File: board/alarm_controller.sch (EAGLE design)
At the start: 144 parts, among them IC3 AT24C, X1 RJ45-8L21-S, X2 RJ45-8L21-S

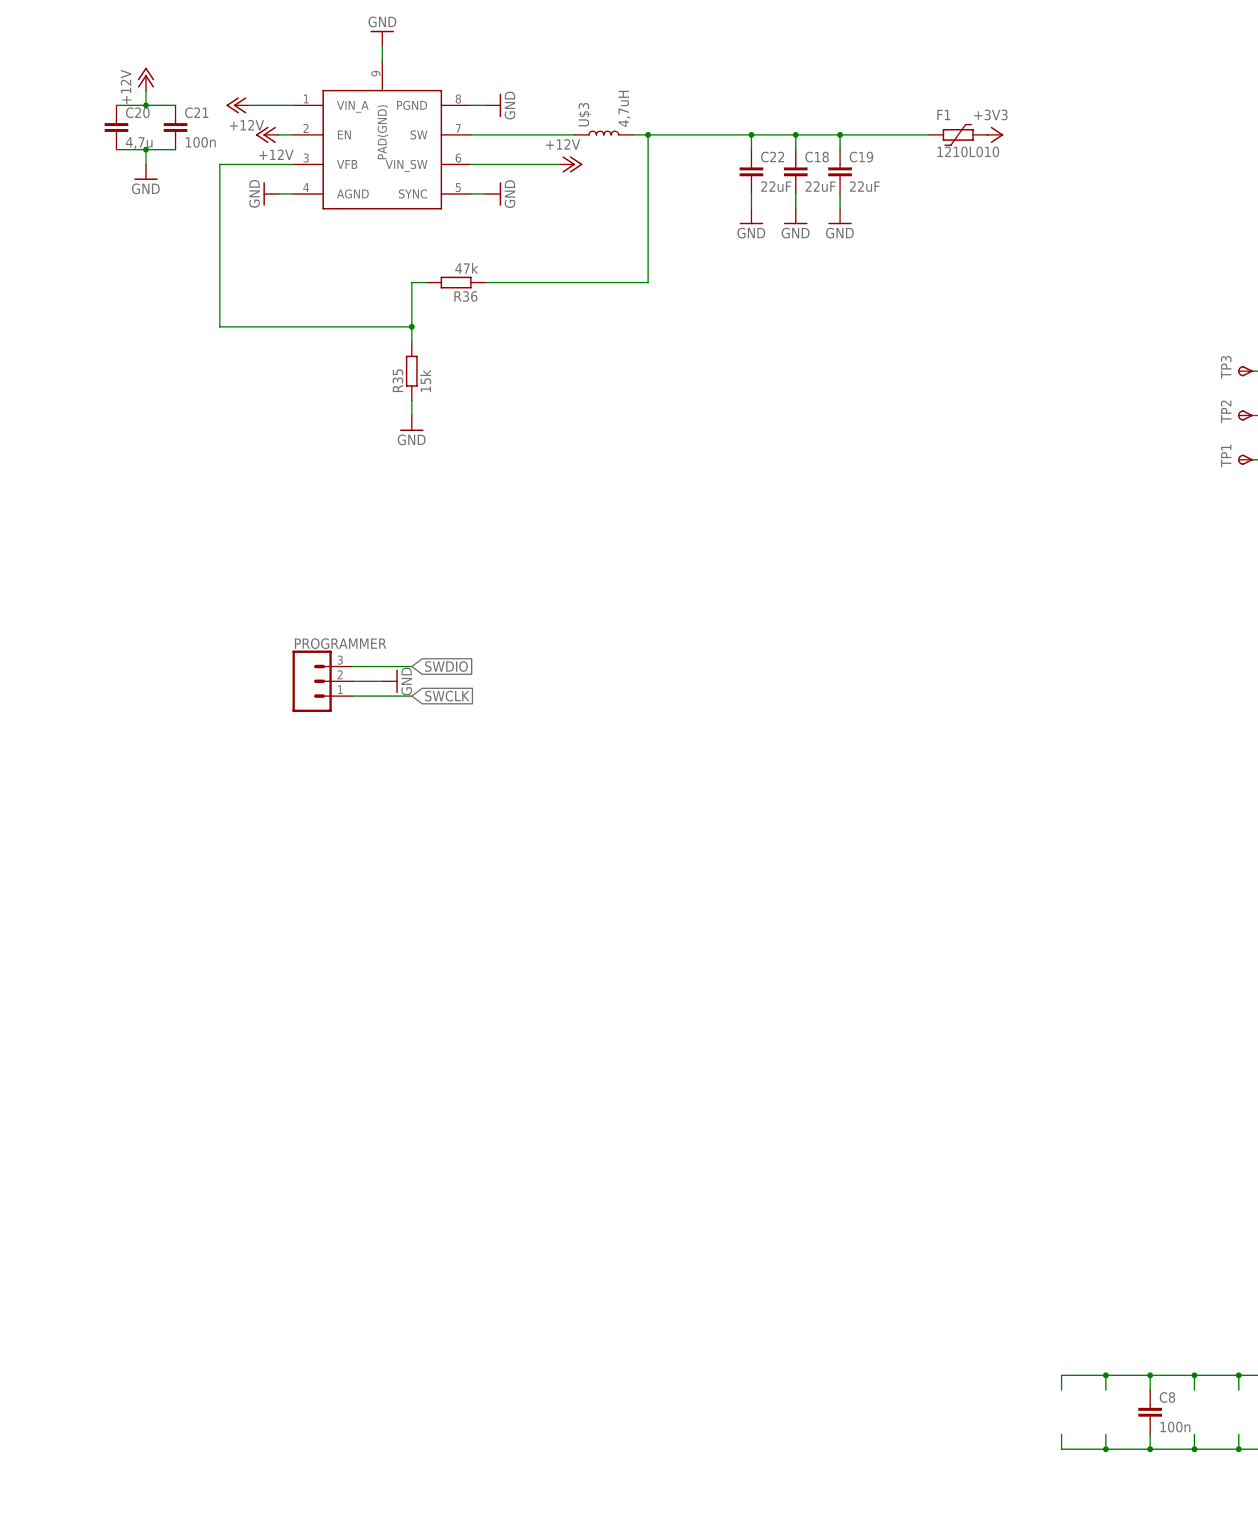
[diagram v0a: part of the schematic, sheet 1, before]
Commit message: change to premade power supply
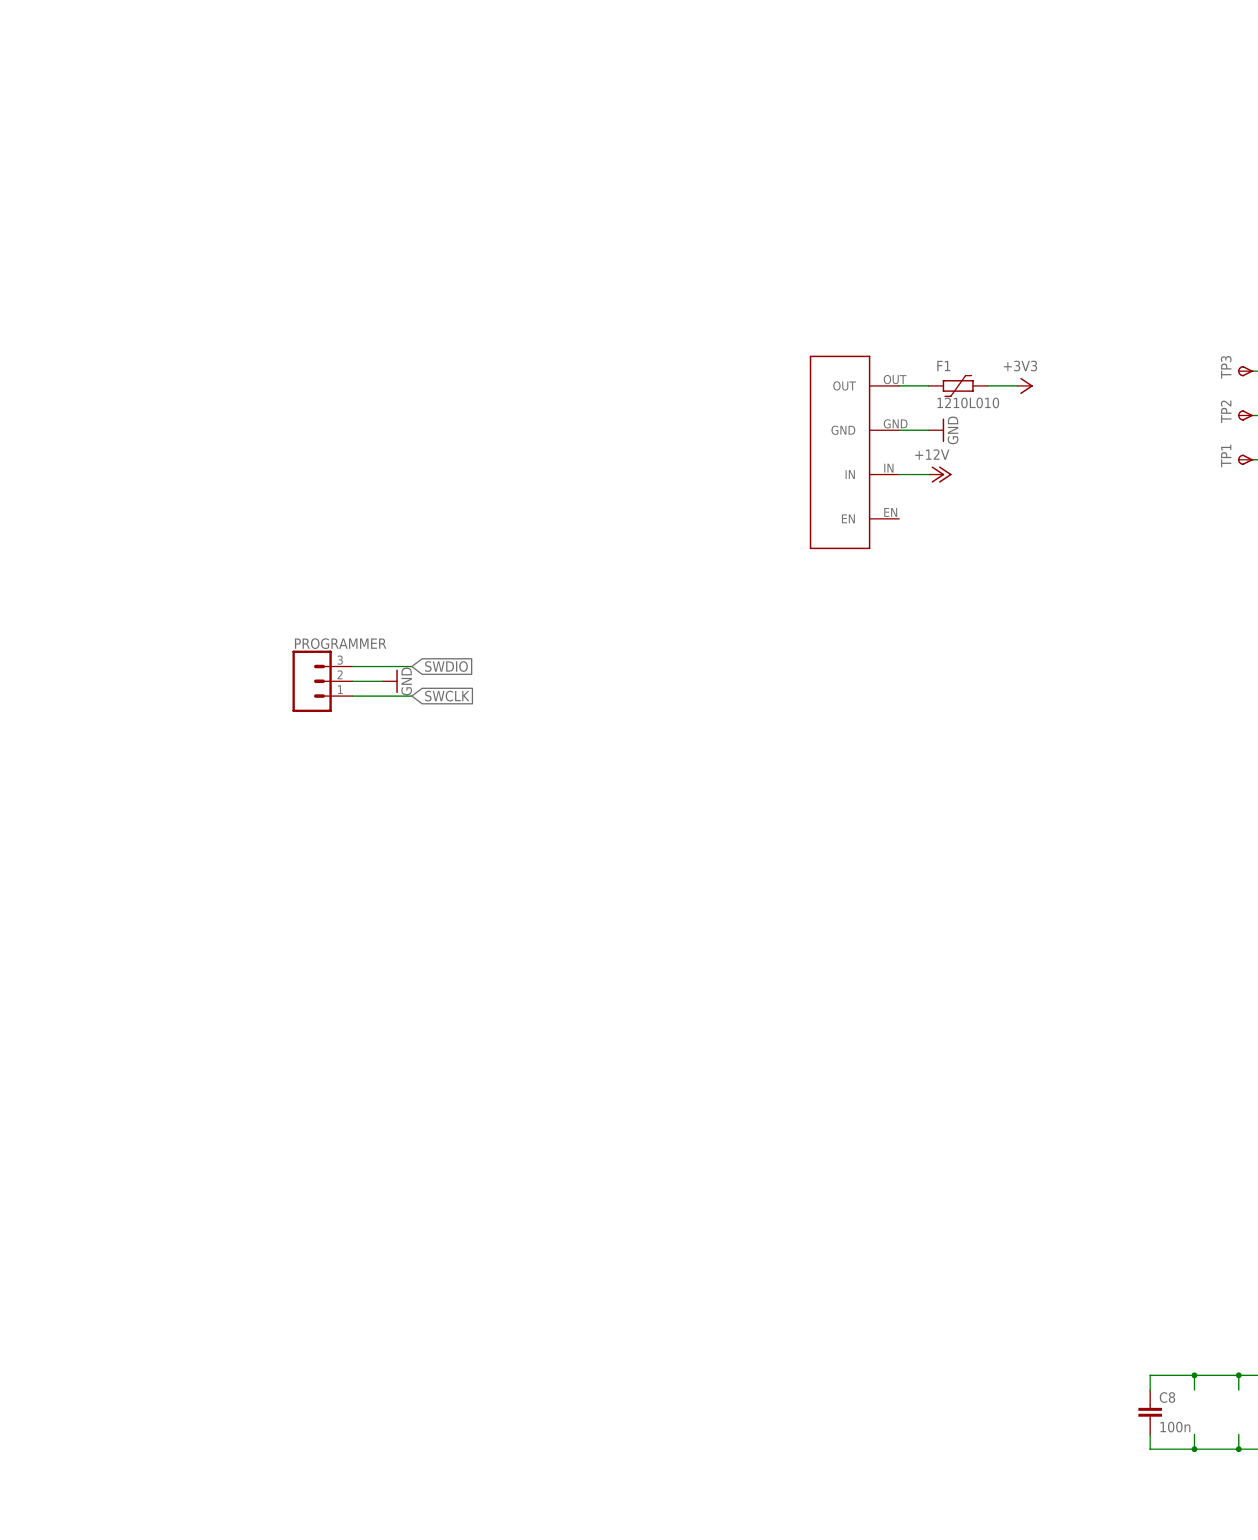
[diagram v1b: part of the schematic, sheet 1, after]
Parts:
- removed C18, C19, C22: 22uF, rcl:C-EUC0805
- removed C20: 4,7u, rcl:C-EUC1206
- removed C21: 100n, rcl:C-EUC0603
- removed R35: 15k, rcl:R-EU_R0603
- removed R36: 47k, rcl:R-EU_R0603
- removed U$2: ST1S10, lcd:ST1S10
- removed U$3: 4,7uH, lcd:PCD0504MT4R7
- added U$4: HW-613, components:HW-613
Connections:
- removed net N$13: C18.1, C19.1, C22.1, F1.2, R36.1, U$3.2
- removed net N$7: U$2.SW, U$3.1
- net +12V: now also U$4.IN; no longer C20.1, C21.1, U$2.EN, U$2.VIN_A, U$2.VIN_SW
- net GND: now also U$4.GND; no longer C18.2, C19.2, C20.2, C21.2, C22.2, R35.1, U$2.AGND, U$2.PAD(GND), U$2.PGND, U$2.SYNC
- net N$3: now also F1.2, U$4.OUT; no longer R35.2, R36.2, U$2.VFB
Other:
- moved on the sheet: F1

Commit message: add reset button
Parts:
- added S1: (no value), SparkFun-Switches:MOMENTARY-SWITCH-SPST-2-SMD-4.6X2.8MM
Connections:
- removed net N$5: R1.2, U$1.NRST
- new net N$7: R1.2, S1.3, S1.4, U$1.NRST
- net GND: now also S1.1, S1.2

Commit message: fix tamper
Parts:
- added J1: (no value), SparkFun-Connectors:CONN_02
- added R35: 10k, rcl:R-EU_R0603
- added S2: (no value), SparkFun-Switches:MOMENTARY-SWITCH-SPST-2-SMD-4.6X2.8MM
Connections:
- new net HARDWARE_RESET: R35.2, S2.3, S2.4, U$1.PE0
- new net UART_RX: J1.1, U$1.PA10
- new net UART_TX: J1.2, U$1.PA9
- net +3V3: now also R35.1
- net ASDASD: no longer U$1.PB12
- net GND: now also S2.1, S2.2
- net TAMPER: now also U$1.PB12
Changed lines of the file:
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@@
 <part name="GND15" library="supply1" deviceset="GND" device=""/>
 <part name="S1" library="SparkFun-Switches" deviceset="MOMENTARY-SWITCH-SPST-2" device="-SMD-4.6X2.8MM"/>
+<part name="R35" library="rcl" deviceset="R-EU_" device="R0603" value="10k"/>
+<part name="+3V32" library="supply1" deviceset="+3V3" device=""/>
+<part name="GND16" library="supply1" deviceset="GND" device=""/>
+<part name="S2" library="SparkFun-Switches" deviceset="MOMENTARY-SWITCH-SPST-2" device="-SMD-4.6X2.8MM"/>
+<part name="J1" library="SparkFun-Connectors" deviceset="CONN_02" device=""/>
 </parts>
 <sheets>
@@
 <instance part="GND15" gate="1" x="-45.72" y="129.54" rot="R270"/>
 <instance part="S1" gate="G$1" x="-35.56" y="132.08"/>
+<instance part="R35" gate="G$1" x="104.14" y="142.24" rot="R180"/>
+<instance part="+3V32" gate="G$1" x="114.3" y="142.24" rot="R270"/>
+<instance part="GND16" gate="1" x="116.84" y="137.16" rot="R90"/>
+<instance part="S2" gate="G$1" x="106.68" y="134.62" rot="R180"/>
+<instance part="J1" gate="G$1" x="-142.24" y="86.36"/>
 </instances>
 <busses>
@@
 <wire x1="-43.18" y1="129.54" x2="-40.64" y2="129.54" width="0.1524" layer="91"/>
 </segment>
+<segment>
+<pinref part="GND16" gate="1" pin="GND"/>
+<pinref part="S2" gate="G$1" pin="1"/>
+<pinref part="S2" gate="G$1" pin="2"/>
+<wire x1="111.76" y1="134.62" x2="111.76" y2="137.16" width="0.1524" layer="91"/>
+<junction x="111.76" y="137.16"/>
+<wire x1="114.3" y1="137.16" x2="111.76" y2="137.16" width="0.1524" layer="91"/>
+</segment>
 </net>
 <net name="CAN_TX" class="0">
@@
 <pinref part="PAD1" gate="G$1" pin="P"/>
 </segment>
+<segment>
+<pinref part="+3V32" gate="G$1" pin="+3V3"/>
+<pinref part="R35" gate="G$1" pin="1"/>
+<wire x1="109.22" y1="142.24" x2="111.76" y2="142.24" width="0.1524" layer="91"/>
+</segment>
 </net>
 <net name="N$4" class="0">
@@
 </segment>
 </net>
-<net name="ASDASD" class="0">
-<segment>
-<pinref part="U$1" gate="G$1" pin="PB12"/>
-<wire x1="-45.72" y1="30.48" x2="-71.12" y2="30.48" width="0.1524" layer="91"/>
-<label x="-71.12" y="30.48" size="1.778" layer="95" rot="R180" xref="yes"/>
-</segment>
-</net>
 <net name="N$7" class="0">
 <segment>
@@
 </segment>
 </net>
+<net name="TAMPER" class="0">
+<segment>
+<pinref part="U$1" gate="G$1" pin="PB12"/>
+<wire x1="-45.72" y1="30.48" x2="-71.12" y2="30.48" width="0.1524" layer="91"/>
+<label x="-71.12" y="30.48" size="1.778" layer="95" rot="R180" xref="yes"/>
+</segment>
+</net>
+<net name="UART_RX" class="0">
+<segment>
+<pinref part="U$1" gate="G$1" pin="PA10"/>
+<wire x1="-45.72" y1="78.74" x2="-55.88" y2="78.74" width="0.1524" layer="91"/>
+<label x="-55.88" y="78.74" size="1.778" layer="95" rot="R180" xref="yes"/>
+</segment>
+<segment>
+<pinref part="J1" gate="G$1" pin="1"/>
+<wire x1="-134.62" y1="86.36" x2="-119.38" y2="86.36" width="0.1524" layer="91"/>
+<label x="-119.38" y="86.36" size="1.778" layer="95" xref="yes"/>
+</segment>
+</net>
+<net name="UART_TX" class="0">
+<segment>
+<pinref part="U$1" gate="G$1" pin="PA9"/>
+<wire x1="-45.72" y1="81.28" x2="-60.96" y2="81.28" width="0.1524" layer="91"/>
+<label x="-60.96" y="81.28" size="1.778" layer="95" rot="R180" xref="yes"/>
+</segment>
+<segment>
+<pinref part="J1" gate="G$1" pin="2"/>
+<wire x1="-134.62" y1="88.9" x2="-124.46" y2="88.9" width="0.1524" layer="91"/>
+<label x="-124.46" y="88.9" size="1.778" layer="95" xref="yes"/>
+</segment>
+</net>
+<net name="HARDWARE_RESET" class="0">
+<segment>
+<pinref part="S2" gate="G$1" pin="3"/>
+<pinref part="S2" gate="G$1" pin="4"/>
+<wire x1="101.6" y1="134.62" x2="101.6" y2="137.16" width="0.1524" layer="91"/>
+<pinref part="R35" gate="G$1" pin="2"/>
+<wire x1="97.79" y1="142.24" x2="99.06" y2="142.24" width="0.1524" layer="91"/>
+<wire x1="101.6" y1="137.16" x2="97.79" y2="137.16" width="0.1524" layer="91"/>
+<wire x1="97.79" y1="137.16" x2="97.79" y2="142.24" width="0.1524" layer="91"/>
+<junction x="101.6" y="137.16"/>
+<wire x1="76.2" y1="142.24" x2="97.79" y2="142.24" width="0.1524" layer="91"/>
+<junction x="97.79" y="142.24"/>
+<label x="76.2" y="142.24" size="1.778" layer="95" rot="R180" xref="yes"/>
+</segment>
+<segment>
+<pinref part="U$1" gate="G$1" pin="PE0"/>
+<wire x1="-12.7" y1="116.84" x2="-12.7" y2="124.46" width="0.1524" layer="91"/>
+<label x="-12.7" y="124.46" size="1.778" layer="95" xref="yes"/>
+</segment>
+</net>

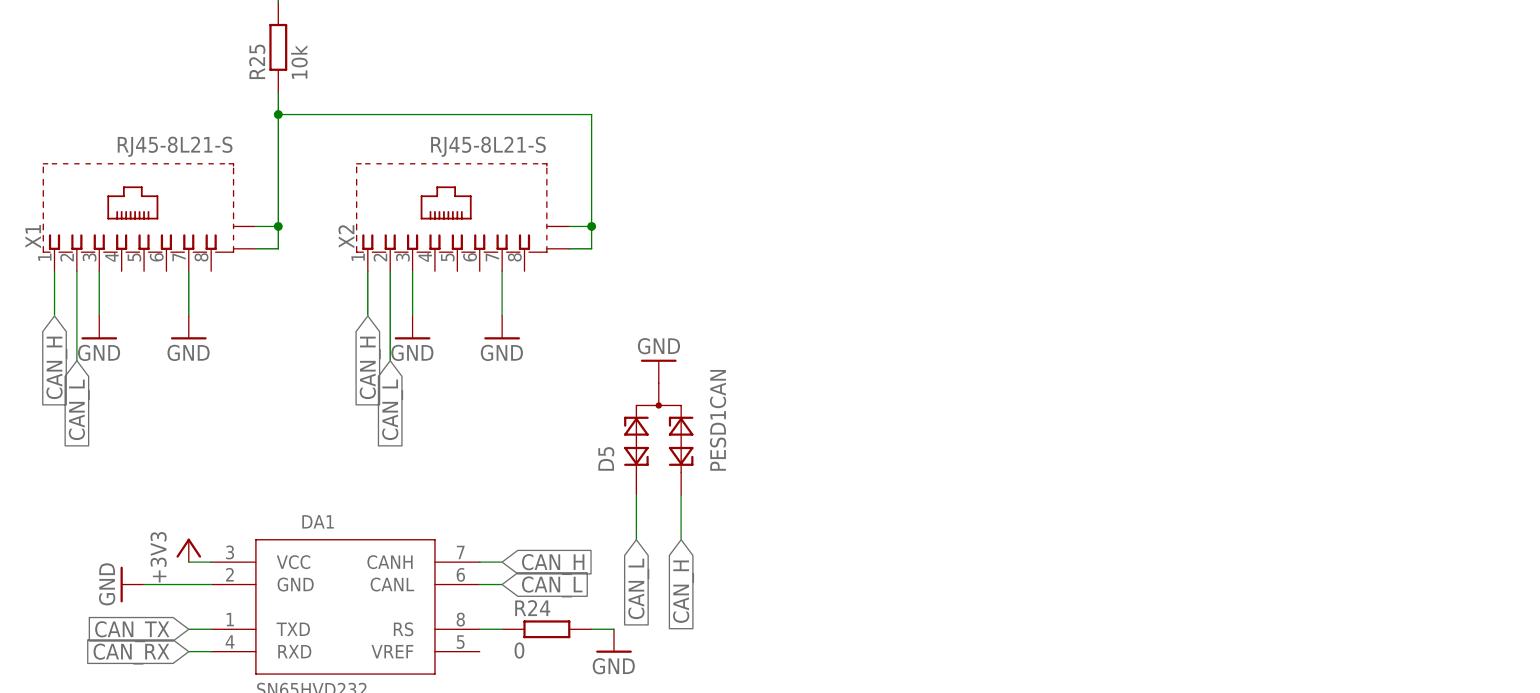
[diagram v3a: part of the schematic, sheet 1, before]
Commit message: power over can
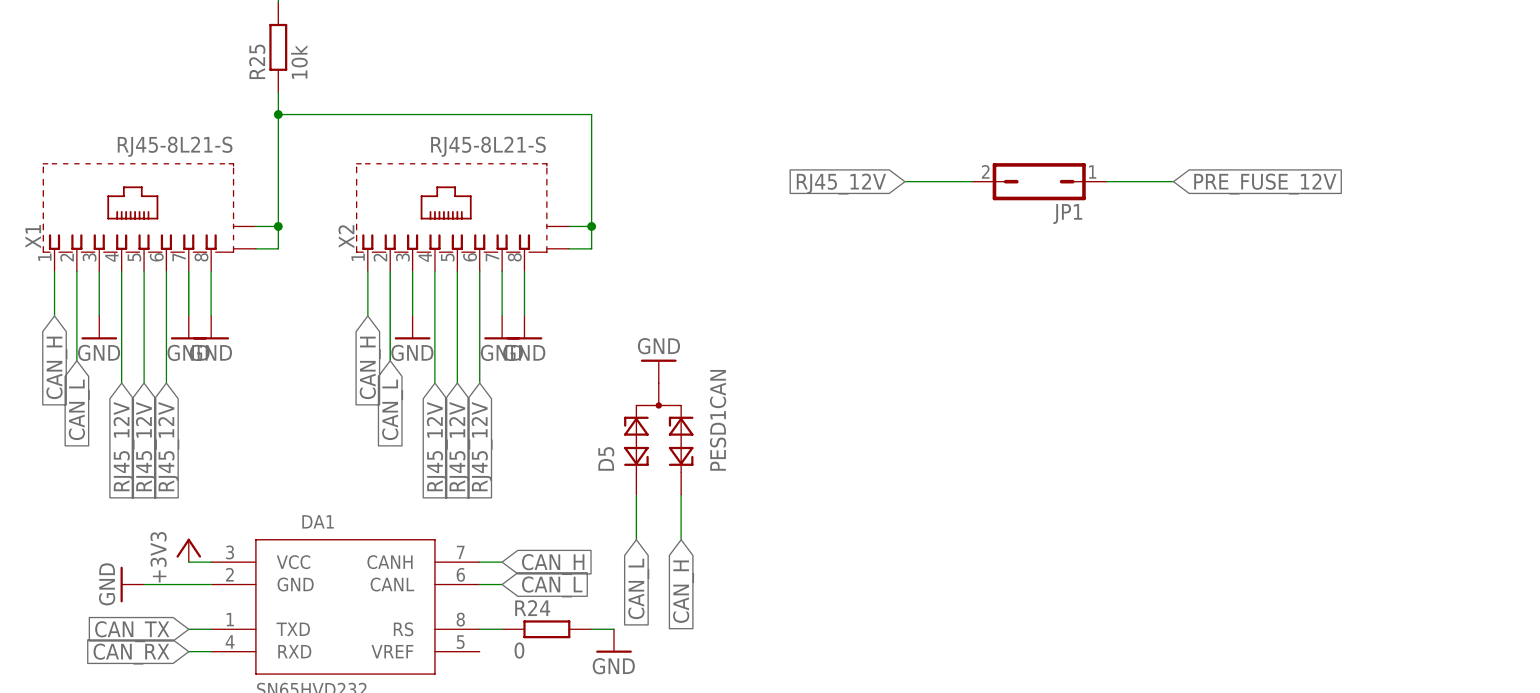
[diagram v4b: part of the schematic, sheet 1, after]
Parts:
- added JP1: (no value), jumper:JP1Q
- C11, C2, C24, C25, C27, C28, C29, C30, C31, C32, C33, C34, C35, C36, C37, C38, C39: device eagle-ltspice:CC0402 -> eagle-ltspice:CC0603
- R10, R11, R12, R13, R14, R15, R16, R17, R18, R19, R20, R21, R22, R23, R26, R28, R29, R30, R31, R32, R33, R34, R37, R38, R39, R40, R41, R42, R43, R44, R45, R46, R47, R48, R49, R50, R51, R52, R53, R54, R55, R56, R57, R58, R59, R6, R60, R61, R62, R7, R8, R9: device rcl:R-EU_R0402 -> rcl:R-EU_R0603
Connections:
- removed net N$14: F2.1, GND8.2
- new net PRE_FUSE_12V: F2.1, GND8.2, JP1.1
- new net RJ45_12V: JP1.2, X1.4, X1.5, X1.6, X2.4, X2.5, X2.6
- net GND: now also X1.8, X2.8

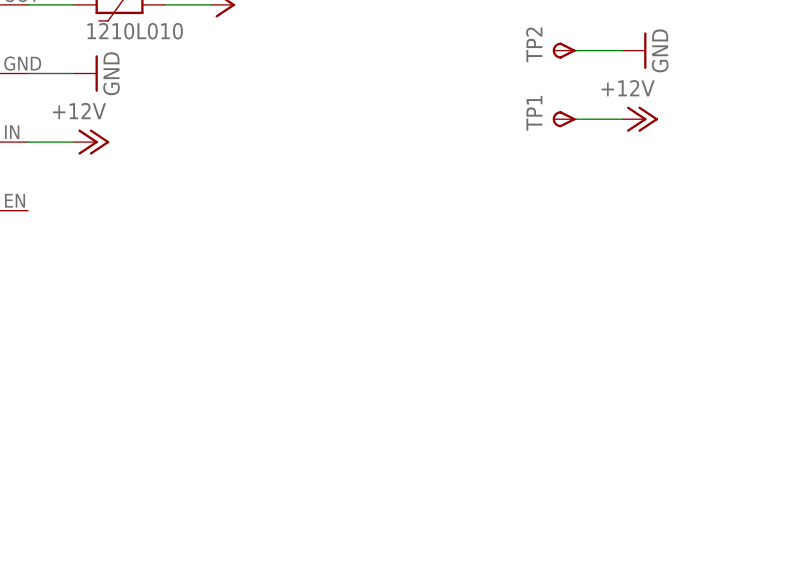
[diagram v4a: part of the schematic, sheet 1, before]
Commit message: add varistor
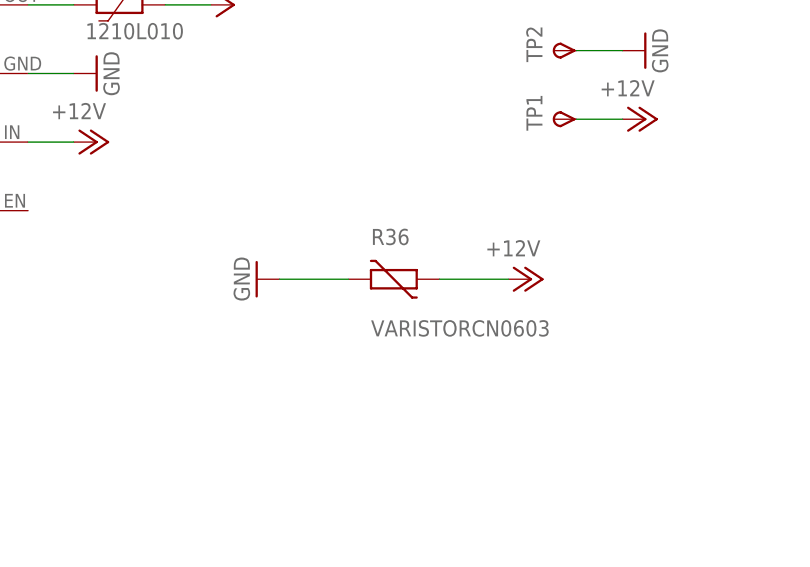
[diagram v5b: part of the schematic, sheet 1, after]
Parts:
- added R36: VARISTORCN0603, varistor:VARISTORCN0603
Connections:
- net +12V: now also R36.1
- net GND: now also R36.2
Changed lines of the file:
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@@
 <part name="GND17" library="supply1" deviceset="GND" device=""/>
 <part name="GND18" library="supply1" deviceset="GND" device=""/>
+<part name="R36" library="varistor" deviceset="VARISTOR" device="CN0603"/>
+<part name="P+1" library="supply1" deviceset="+12V" device=""/>
+<part name="GND19" library="supply1" deviceset="GND" device=""/>
 </parts>
 <sheets>
@@
 <instance part="GND17" gate="1" x="-284.48" y="-20.32"/>
 <instance part="GND18" gate="1" x="-248.92" y="-20.32"/>
+<instance part="R36" gate="G$1" x="-17.78" y="104.14"/>
+<instance part="P+1" gate="1" x="-2.54" y="104.14" rot="R270"/>
+<instance part="GND19" gate="1" x="-33.02" y="104.14" rot="R270"/>
 </instances>
 <busses>
@@
 <pinref part="GND18" gate="1" pin="GND"/>
 </segment>
+<segment>
+<pinref part="R36" gate="G$1" pin="2"/>
+<pinref part="GND19" gate="1" pin="GND"/>
+<wire x1="-30.48" y1="104.14" x2="-22.86" y2="104.14" width="0.1524" layer="91"/>
+</segment>
 </net>
 <net name="+3V3" class="0">
@@
 <wire x1="-58.42" y1="119.38" x2="-53.34" y2="119.38" width="0.1524" layer="91"/>
 </segment>
+<segment>
+<pinref part="R36" gate="G$1" pin="1"/>
+<pinref part="P+1" gate="1" pin="+12V"/>
+<wire x1="-5.08" y1="104.14" x2="-12.7" y2="104.14" width="0.1524" layer="91"/>
+</segment>
 </net>
